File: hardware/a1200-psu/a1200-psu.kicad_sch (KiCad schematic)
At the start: 58 parts, among them J1 220V, J2 Conn_01x05, Q1 BC327, Q2 BC327, Q3 BU508AF, SW1 SW_SPST, U2 TL431D, U3 UC3844_DIP8

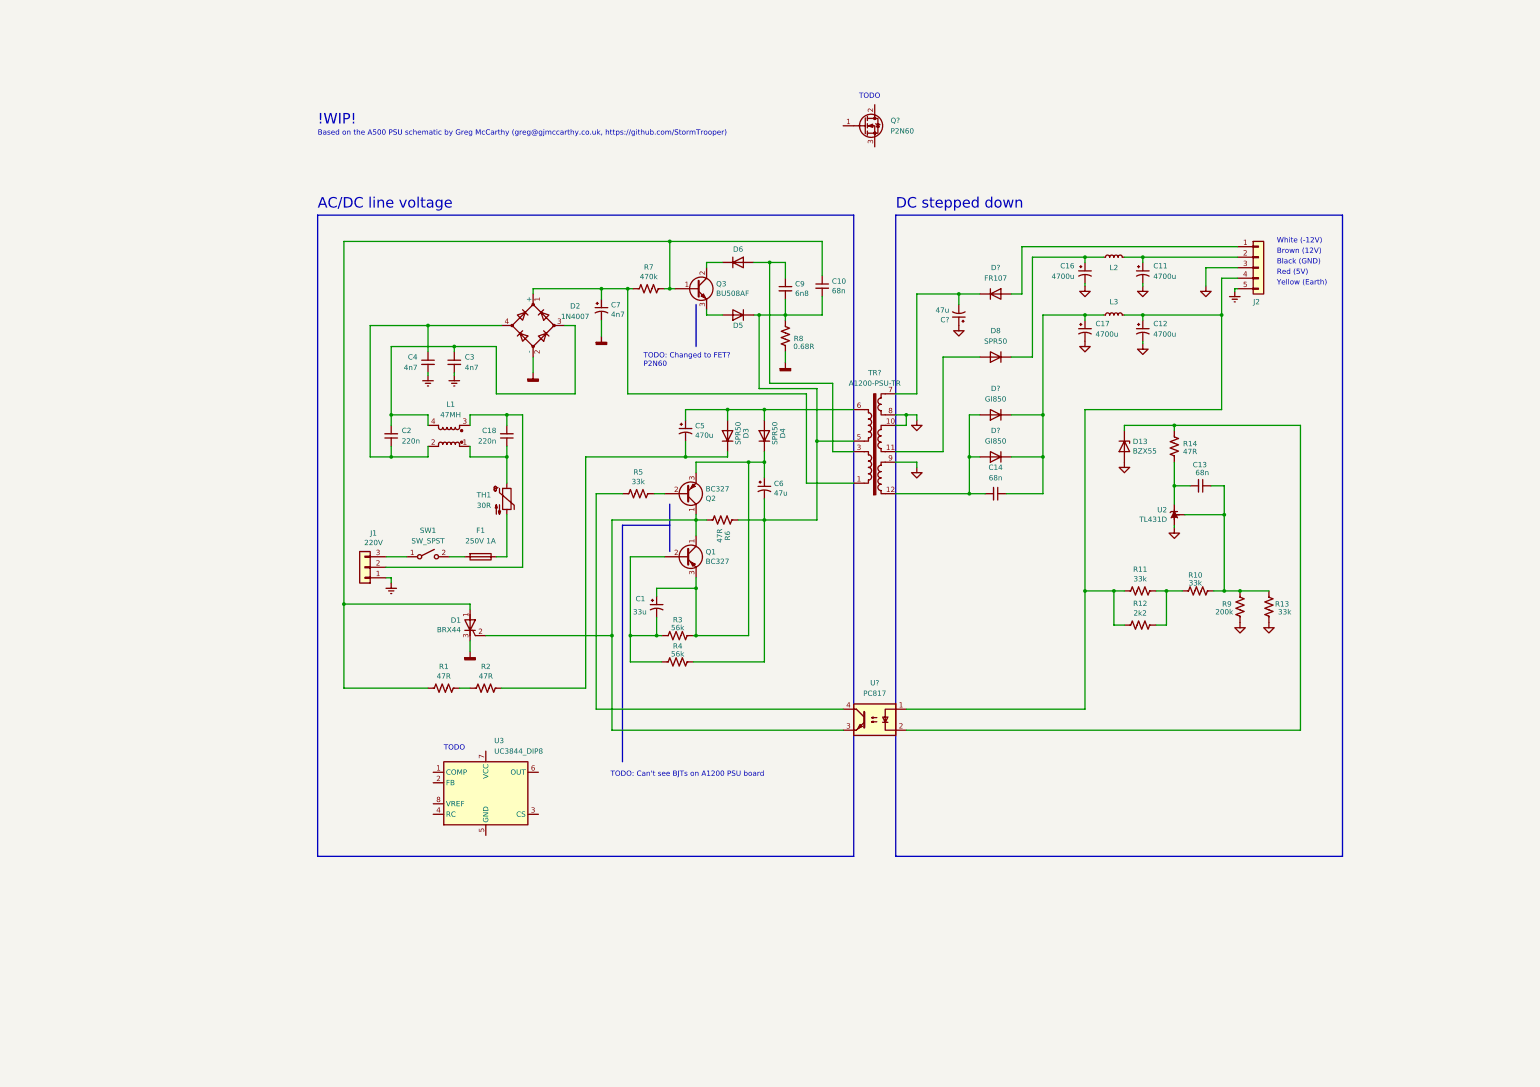
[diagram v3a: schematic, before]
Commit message: Started on P2N60 + UC3844_DIP8
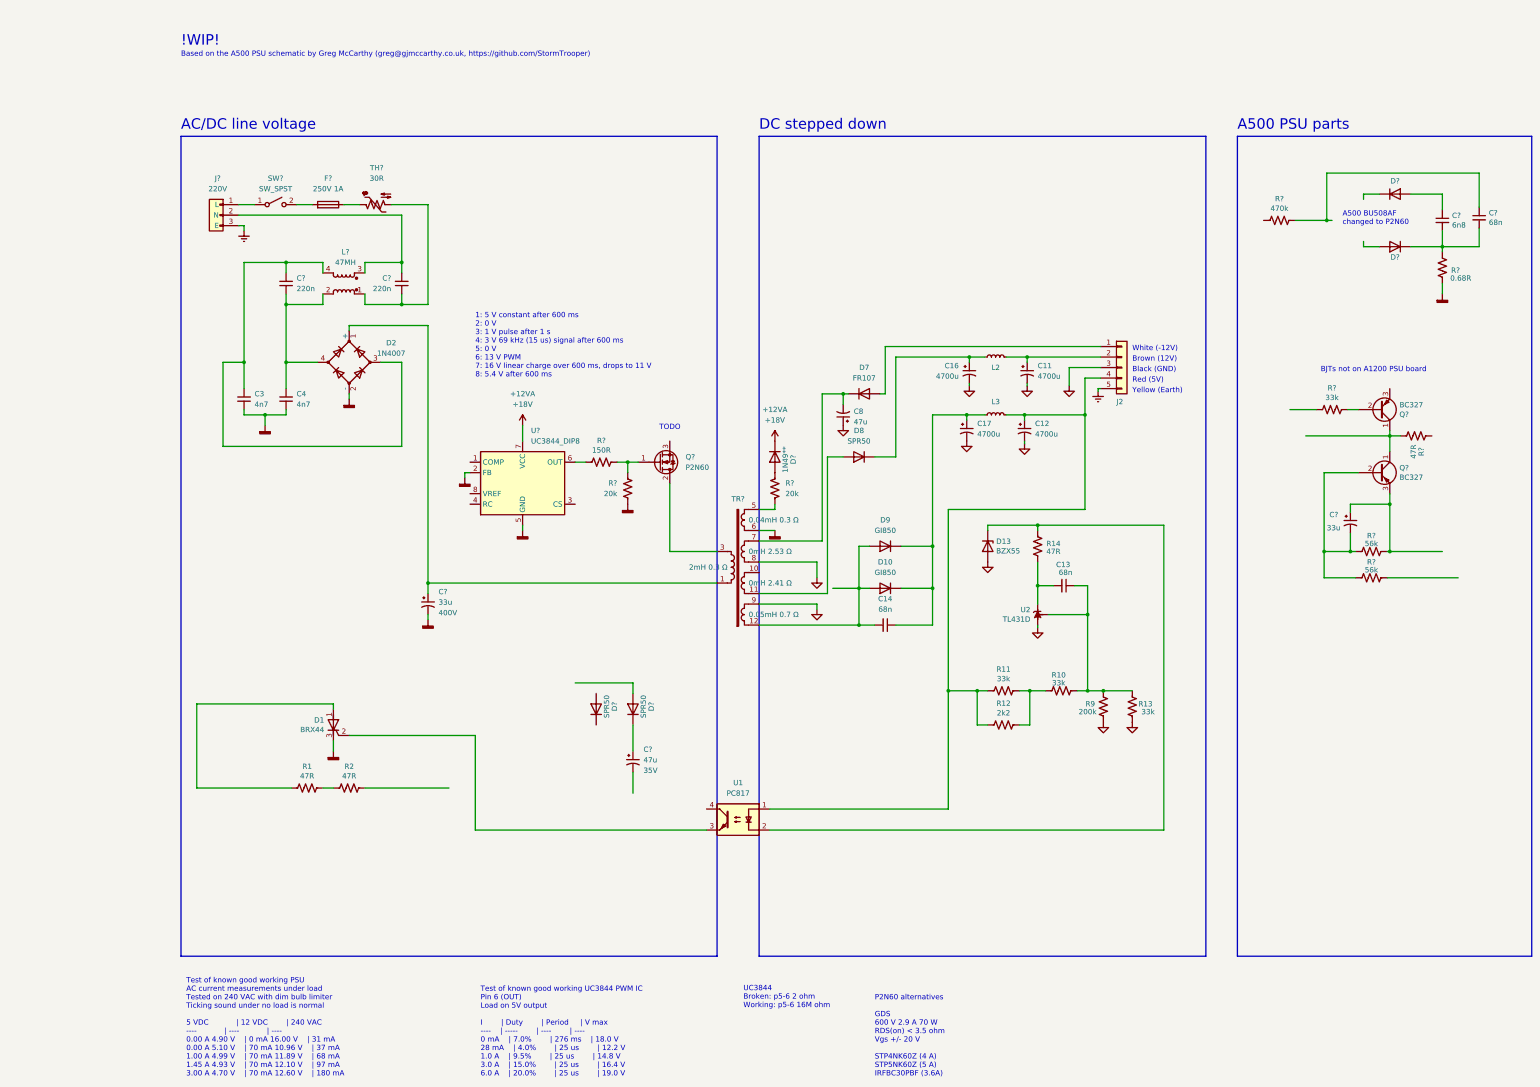
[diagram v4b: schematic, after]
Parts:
- removed C1: 33u, symbol a500-psu-rescue:CP1_Small-Device
- removed C10: 68n, symbol Device:C_Small
- removed C18, C2: 220n, symbol Device:C_Small
- removed C5: 470u, symbol a500-psu-rescue:CP1_Small-Device
- removed C6: 47u, symbol a500-psu-rescue:CP1_Small-Device
- removed C7: 4n7, symbol a500-psu-rescue:CP1_Small-Device
- removed C9: 6n8, symbol Device:C_Small
- removed D3, D4: SPR50, symbol Device:D
- removed D5, D6: FR107, symbol Device:D
- removed F1: 250V 1A, symbol Device:Fuse
- removed J1: 220V, symbol Connector_Generic:Conn_01x03
- removed L1: 47MH, symbol Device:L_Coupled
- removed Q1, Q2: BC327, Package_TO_SOT_THT:TO-92_Inline, symbol Transistor_BJT:BC327
- removed Q3: BU508AF, symbol Device:Q_NPN_BCE
- removed Q?: P2N60, Package_TO_SOT_THT:TO-220-3_Vertical, symbol Device:Q_NMOS_GDS
- removed R3, R4: 56k, symbol Device:R_US
- removed R5: 33k, symbol Device:R_US
- removed R6: 47R, symbol Device:R_US
- removed R7: 470k, symbol Device:R_US
- removed R8: 0.68R, symbol Device:R_US
- removed SW1: SW_SPST, symbol Switch:SW_SPST
- removed TH1: 30R, symbol Device:Thermistor_NTC
- removed TR?: A1200-PSU-TR, symbol Amiga A1200:A1200-PSU-TR
- removed U3: UC3844_DIP8, Package_DIP:DIP-8_W7.62mm, symbol Regulator_Controller:UC3844_DIP8
- added C? (x2): 33u, symbol a500-psu-rescue:CP1_Small-Device
- added C?: 47u, symbol a500-psu-rescue:CP1_Small-Device
- added C? (x2): 220n, symbol Device:C_Small
- added C?: 68n, symbol Device:C_Small
- added C?: 6n8, symbol Device:C_Small
- added D? (x2): FR107, symbol Device:D
- added D? (x2): SPR50, symbol Device:D
- added D?: 1N49**, symbol Device:D
- added F?: 250V 1A, symbol Device:Fuse
- added J?: 220V, symbol Amiga A1200:AC_IN
- added L?: 47MH, symbol Device:L_Coupled
- added Q? (x2): BC327, Package_TO_SOT_THT:TO-92_Inline, symbol Transistor_BJT:BC327
- added Q?: P2N60, Package_TO_SOT_THT:TO-220-3_Vertical, symbol Device:Q_NMOS_GDS
- added R?: 47R, symbol Device:R_US
- added R?: 470k, symbol Device:R_US
- added R? (x2): 56k, symbol Device:R_US
- added R? (x2): 20k, symbol Device:R_US
- added R?: 33k, symbol Device:R_US
- added R?: 150R, symbol Device:R_US
- added R?: 0.68R, symbol Device:R_US
- added SW?: SW_SPST, symbol Switch:SW_SPST
- added TH?: 30R, symbol Device:Thermistor_NTC_US
- added TR?: A1200-PSU-TR, Transformer_THT:Transformer_CHK_EI48-8VA_Neutral, symbol Amiga 1200:A1200-PSU-TR
- added U?: UC3844_DIP8, Package_DIP:DIP-8_W7.62mm, symbol Regulator_Controller:UC3844_DIP8
- gave numbers to parts that had none: 5
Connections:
- net Earth: now also J?.3 (E); no longer C3.2, C4.2
- net GND: now also TR?.8, TR?.9
- net GNDD: now also C3.2, C4.2, C?.2, R?.1, R?.2, TR?.6, U?.2 (FB), U?.5 (GND)
- net at C3.1, D2.3: now also C?.2, L?.4
- net at D2.1 (+): now also C?.1, TR?.1
- net at C4.1, D2.4: now also C?.1, L?.2
- net at D8.2 (A): now also TR?.11
- net at C14.2, D10.2 (A), D9.2 (A): now also TR?.12
- net at C8.2, D7.1 (K): now also TR?.7
- new net: Q?.1 (C), Q?.1 (C), R?.1
- new net: C?.1, R?.1
- new net: C?.2, C?.2, D?.1 (K), R?.2
- new net: C?.2, Q?.2 (B), R?.2, R?.2
- new net: C?.1, Q?.3 (E), R?.1
- new net: Q?.2 (B), R?.1
- new net: F?.1, TH?.1
- new net: F?.2, SW?.2 (B)
- new net: Q?.2 (D), TR?.3
- new net: R?.2, TR?.5
- new net: C?.1, D?.1 (K)
- new net: C?.1, L?.1, TH?.2
- new net: C?.2, J?.2 (N), L?.3
- new net: C?.1, D?.2 (A)
- new net: Q?.1 (G), R?.1, R?.1
- new net: D?.2 (A), R?.1
- new net: R?.2, U?.6 (OUT)
- new net: J?.1 (L), SW?.1 (A)
- new net +12VA: D?.1 (K), U?.7 (VCC)
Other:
- note added: "1: 5 V constant after 600 ms 2: 0 V 3: 1 V pulse after 1 s 4: 3 V 69 kHz (15 us) signal after 600 ms 5: 0 V 6: 13 V PWM 7: 16 V linear charge over 600 ms, drops to 11 V 8: 5.4 V after 600 ms"
- note added: "A500 BU508AF changed to P2N60"
- note added: "A500 PSU parts"
- note added: "BJTs not on A1200 PSU board"
- note added: "P2N60 alternatives GDS 600 V 2.9 A 70 W RDS(on) < 3.5 ohm Vgs +/- 20 V STP4NK60Z (4 A) STP5NK60Z (5 A) IRFBC30PBF (3.6A)"
- note added: "Test of known good working PSU AC current measurements under load Tested on 240 VAC with dim bulb limiter Ticking sound under no load is normal 5 VDC | 12 VDC | 240 VAC ---- | ---- | ---- 0.00 A 4.90 V | 0 mA 16.00 V | 31 mA 0.00 A 5.10 V | 70 mA 10.96 V | 37 mA 1.00 A 4.99 V | 70 mA 11.89 V | 68 mA 1.45 A 4.93 V | 70 mA 12.10 V | 97 mA 3.00 A 4.70 V | 70 mA 12.60 V | 180 mA"
- note added: "Test of known good working UC3844 PWM IC Pin 6 (OUT) Load on 5V output I | Duty | Period | V max ---- | ----- | ---- | ---- 0 mA | 7.0% | 276 ms | 18.0 V 28 mA | 4.0% | 25 us | 12.2 V 1.0 A | 9.5% | 25 us | 14.8 V 3.0 A | 15.0% | 25 us | 16.4 V 6.0 A | 20.0% | 25 us | 19.0 V"
- note added: "UC3844 Broken: p5-6 2 ohm Working: p5-6 16M ohm"
- note removed: "TODO: Can't see BJTs on A1200 PSU board"
- note removed: "TODO: Changed to FET? P2N60"
- title: Commodore A1200 Power Supply  391029-02 -> Amiga A1200 PSU UK 391029-02
- moved on the sheet: C11, C12, C13, C14, C16, C17, C3, C4, C8, D1, D10, D13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

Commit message: Reorganised line side
Also made some corrections for stepped down side
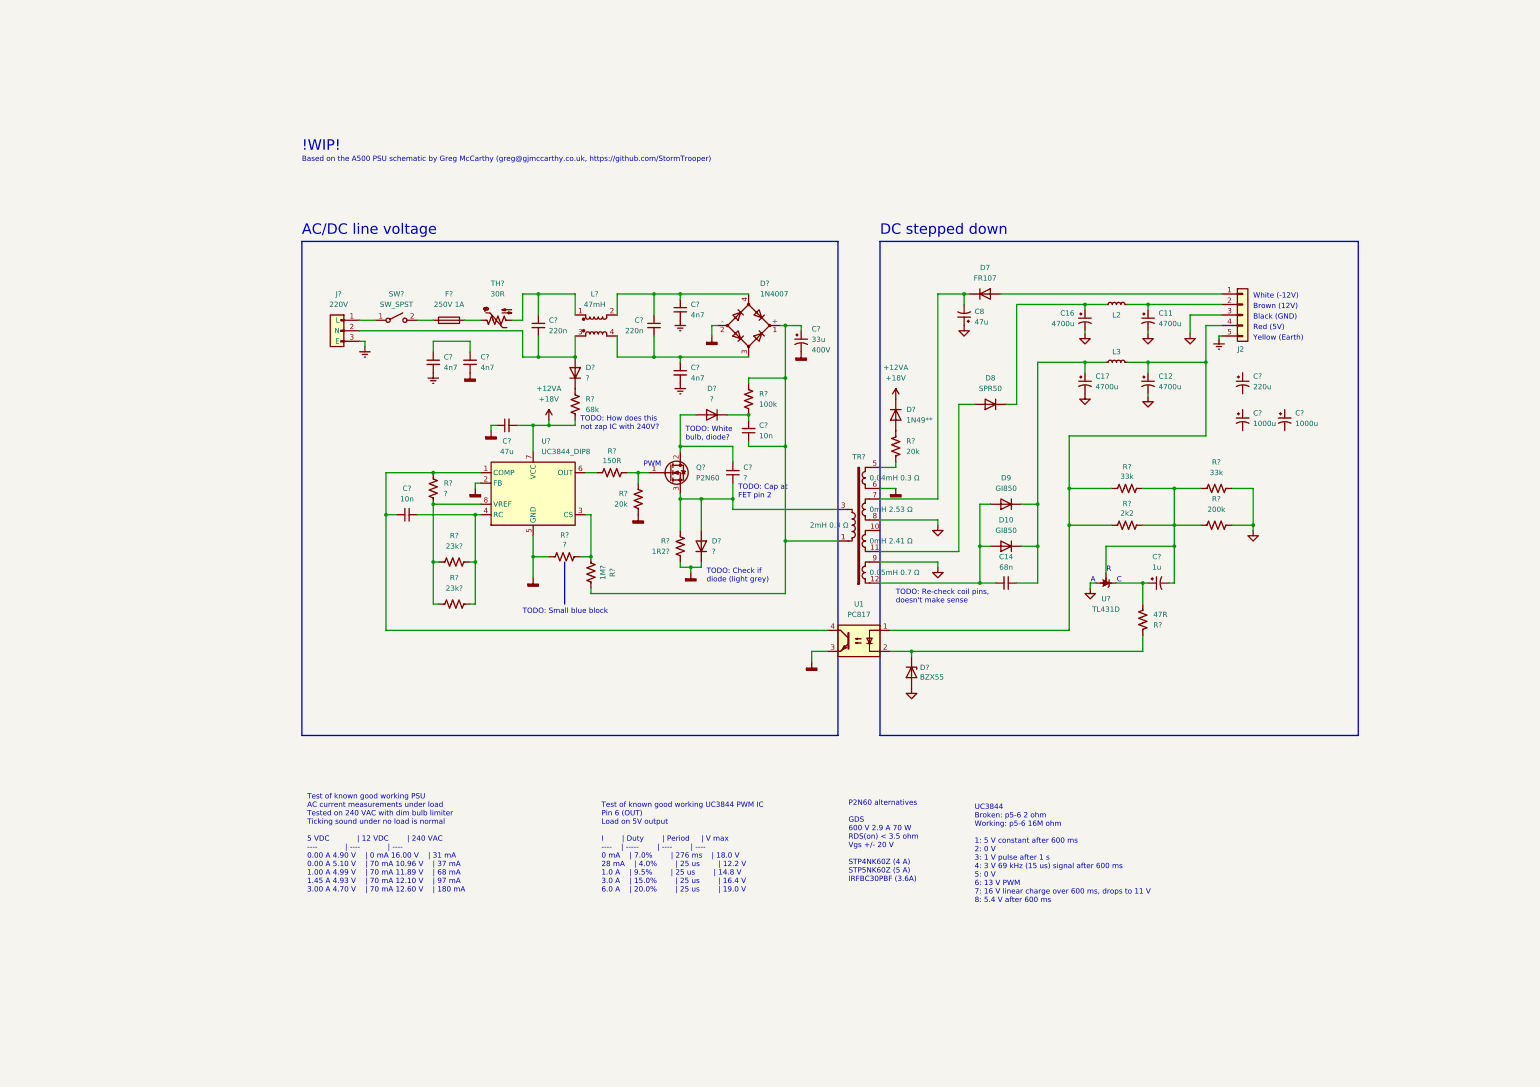
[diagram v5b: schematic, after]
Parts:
- removed C13, C?: 68n, symbol Device:C_Small
- removed C3, C4: 4n7, symbol Device:C_Small
- removed C? (x2): 33u, symbol a500-psu-rescue:CP1_Small-Device
- removed C?: 47u, symbol a500-psu-rescue:CP1_Small-Device
- removed C? (x2): 220n, symbol Device:C_Small
- removed C?: 6n8, symbol Device:C_Small
- removed D1: BRX44, symbol Device:Q_SCR_AGK
- removed D13: BZX55, symbol Device:D_Zener
- removed D2: 1N4007, symbol Device:D_Bridge_+-AA
- removed D? (x2): FR107, symbol Device:D
- removed D? (x2): SPR50, symbol Device:D
- removed L?: 47MH, symbol Device:L_Coupled
- removed Q? (x2): BC327, Package_TO_SOT_THT:TO-92_Inline, symbol Transistor_BJT:BC327
- removed R1, R14, R2, R?: 47R, symbol Device:R_US
- removed R10, R11, R13, R?: 33k, symbol Device:R_US
- removed R12: 2k2, symbol Device:R_US
- removed R9: 200k, symbol Device:R_US
- removed R?: 470k, symbol Device:R_US
- removed R? (x2): 56k, symbol Device:R_US
- removed R?: 0.68R, symbol Device:R_US
- removed U2: TL431D, Package_SO:SOIC-8_3.9x4.9mm_P1.27mm, symbol Reference_Voltage:TL431D
- added C?: 33u, symbol a500-psu-rescue:CP1_Small-Device
- added C? (x2): 10n, symbol Device:C_Small
- added C?: 1u, symbol a500-psu-rescue:CP1_Small-Device
- added C?: 220u, symbol a500-psu-rescue:CP1_Small-Device
- added C?: 47u, symbol Device:C_Small
- added C? (x2): 1000u, symbol a500-psu-rescue:CP1_Small-Device
- added C? (x2): 220n, symbol Device:C_Small
- added C? (x4): 4n7, symbol Device:C_Small
- added C?: ?, symbol Device:C_Small
- added D?: BZX55, symbol Device:D_Zener
- added D? (x3): ?, symbol Device:D
- added D?: 1N4007, symbol Device:D_Bridge_+-AA
- added L?: 47mH, symbol Device:L_Coupled
- added R? (x2): 23k?, symbol Device:R_US
- added R?: 100k, symbol Device:R_US
- added R?: 1R2?, symbol Device:R_US
- added R?: 1M?, symbol Device:R_US
- added R? (x2): ?, symbol Device:R_US
- added R?: 68k, symbol Device:R_US
- added R? (x2): 33k, symbol Device:R_US
- added R?: 47R, symbol Device:R_US
- added R?: 200k, symbol Device:R_US
- added R?: 2k2, symbol Device:R_US
- added U?: TL431D, Package_SO:SOIC-8_3.9x4.9mm_P1.27mm, symbol Reference_Voltage:TL431D
- TR?: 1-3 2mH 0.3 Ω -> (none); 10-11 0mH 2.53 Ω -> (none); 6-5 0.05mH 0.7 Ω -> (none); 7-8 0.04mH 0.3 Ω -> (none); 9-12 0mH 2.41 Ω -> (none); Value 1-3 (none) -> 2mH 0.3 Ω; Value 10-11 (none) -> 0mH 2.53 Ω; Value 6-5 (none) -> 0.05mH 0.7 Ω; Value 7-8 (none) -> 0.04mH 0.3 Ω; Value 9-12 (none) -> 0mH 2.41 Ω
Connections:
- net +12VA: now also C?.2, R?.2
- net Earth: now also C?.2, C?.2, C?.2
- net GND: now also D?.2 (A), R?.1, R?.1, U?.2 (A), U?.3 (A), U?.6 (A), U?.7 (A)
- net GNDD: now also U1.3, C?.1, C?.1, C?.2, D?.1 (K), D?.2 (-), R?.2, R?.2
- net at TR?.1: now also C?.1, C?.1, D?.1 (+), R?.1, R?.1
- net at C12.1, J2.4 (Pin_4), L3.2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: now also R?.2, R?.2
- net at U1.2: now also D?.1 (K), R?.2
- net at TR?.3: now also Q?.3 (S), C?.1, D?.2 (A), R?.1; no longer Q?.2 (D)
- net at U1.4: now also U?.1 (COMP), C?.1, R?.2
- net at TH?.2: now also C?.1, L?.1
- net at J?.2 (N): now also C?.2, D?.2 (A), L?.3
- net at U?.3 (CS): now also R?.1, R?.2
- net at U?.4 (RC): now also C?.2, R?.2, R?.2
- net at U?.8 (VREF): now also R?.1, R?.1, R?.1
- new net: C?.2, D?.1 (K), R?.2
- new net: C?.1, R?.1, U?.1 (K)
- new net: C?.2, R?.1, R?.1, R?.2, R?.2, U?.8 (REF)
- new net: C?.1, C?.1, D?.4, L?.2
- new net: C?.1, C?.2, D?.3, L?.4
- new net: C?.1, C?.2
- new net: D?.1 (K), R?.1
- new net: C?.2, D?.2 (A), Q?.2 (D)
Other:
- note added: "A"
- note added: "C"
- note added: "PWM"
- note added: "R"
- note added: "TODO: Cap at FET pin 2"
- note added: "TODO: Check if diode (light grey)"
- note added: "TODO: How does this not zap IC with 240V?"
- note added: "TODO: Re-check coil pins, doesn't make sense"
- note added: "TODO: Small blue block"
- note added: "TODO: White bulb, diode?"
- note added: "UC3844 Broken: p5-6 2 ohm Working: p5-6 16M ohm 1: 5 V constant after 600 ms 2: 0 V 3: 1 V pulse after 1 s 4: 3 V 69 kHz (15 us) signal after 600 ms 5: 0 V 6: 13 V PWM 7: 16 V linear charge over 600 ms, drops to 11 V 8: 5.4 V after 600 ms"
- note removed: "1: 5 V constant after 600 ms 2: 0 V 3: 1 V pulse after 1 s 4: 3 V 69 kHz (15 us) signal after 600 ms 5: 0 V 6: 13 V PWM 7: 16 V linear charge over 600 ms, drops to 11 V 8: 5.4 V after 600 ms"
- note removed: "A500 BU508AF changed to P2N60"
- note removed: "A500 PSU parts"
- note removed: "BJTs not on A1200 PSU board"
- note removed: "TODO"
- note removed: "UC3844 Broken: p5-6 2 ohm Working: p5-6 16M ohm"
- moved on the sheet: C11, C12, C14, C16, C17, C8, D10, D7, D8, D9, D?, F?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
